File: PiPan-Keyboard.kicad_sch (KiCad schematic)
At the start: 89 parts

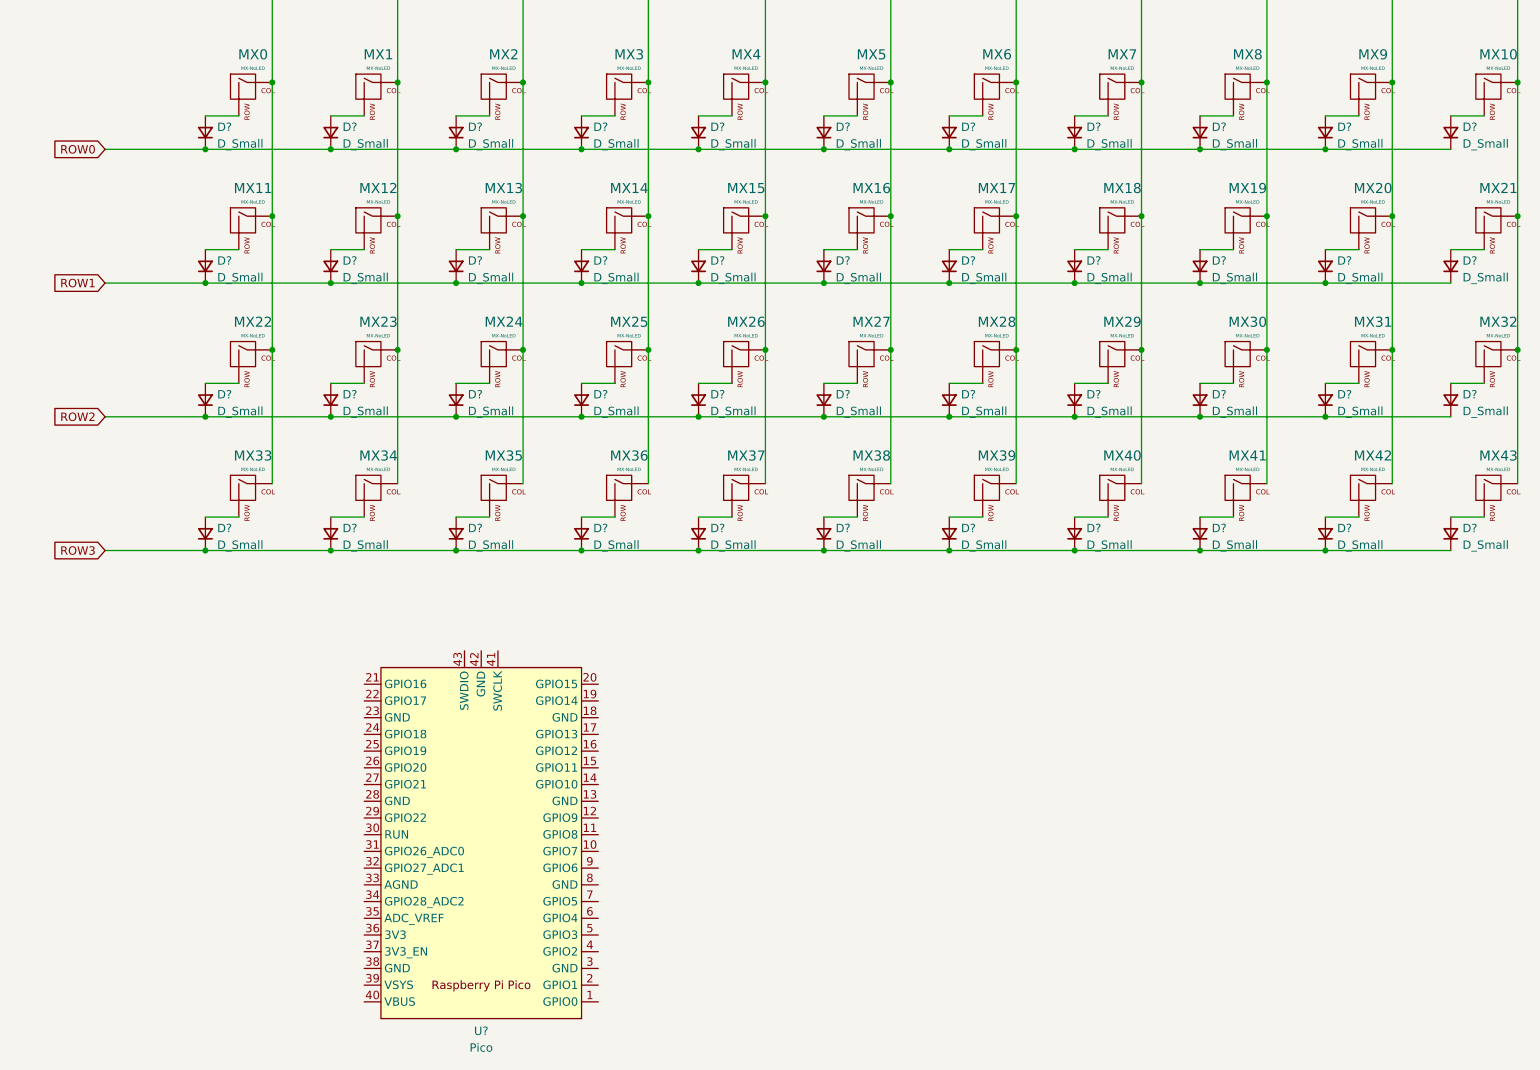
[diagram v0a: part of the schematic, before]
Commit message: added footprints
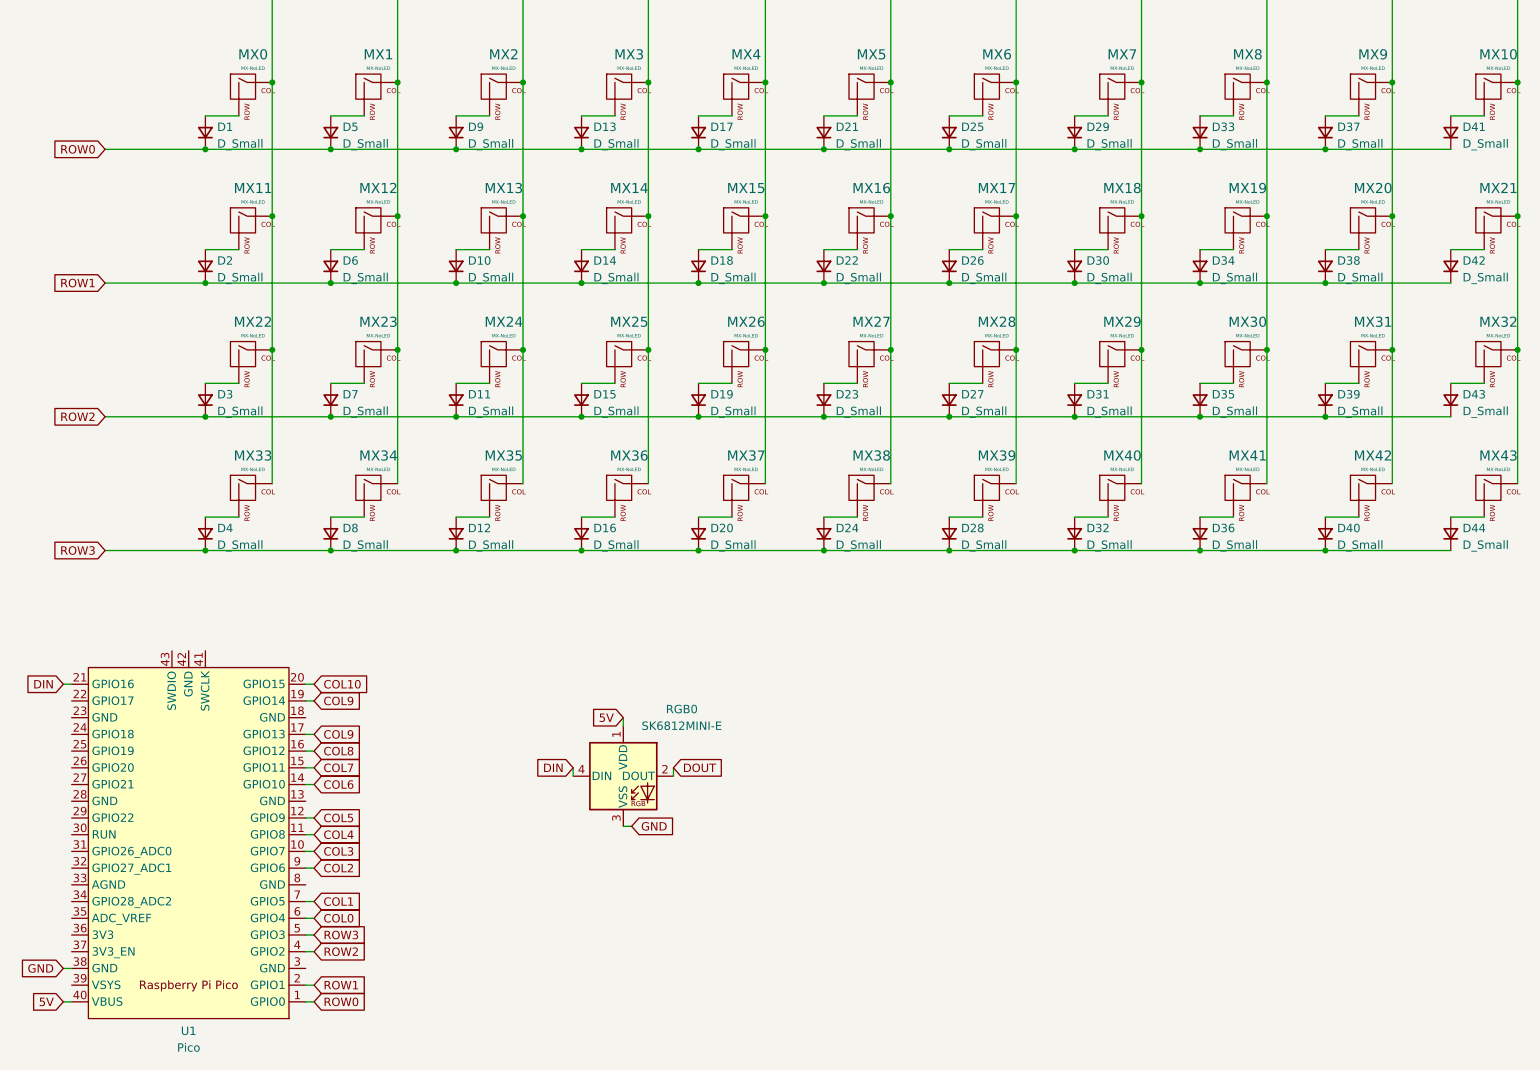
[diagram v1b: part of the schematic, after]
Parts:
- added RGB0: SK6812MINI-E, kicad-keyboard-parts:MX_SK6812MINI-E, symbol kicad-keyboard-parts:SK6812MINI-E
- D1, D10, D11, D12, D13, D14, D15, D16, D17, D18, D19, D2, D20, D21, D22, D23, D24, D25, D26, D27, D28, D29, D3, D30, D31, D32, D33, D34, D35, D36, D37, D38, D39, D4, D40, D41, D42, D43, D44, D5, D6, D7, D8, D9: renamed from D?; footprint (none) -> Diode_THT:D_DO-35_SOD27_P10.16mm_Horizontal
- MX0, MX1, MX10, MX11, MX12, MX13, MX14, MX15, MX16, MX17, MX18, MX19, MX2, MX20, MX21, MX22, MX23, MX24, MX25, MX26, MX27, MX28, MX29, MX3, MX30, MX31, MX32, MX33, MX34, MX35, MX36, MX37, MX38, MX39, MX4, MX40, MX41, MX42, MX43, MX5, MX6, MX7, MX8, MX9: footprint (none) -> keyswitches:Kailh_socket_MX
- U1: renamed from U?; footprint RPi_Pico:RPi_Pico_SMD_TH -> MCU_RaspberryPi_and_Boards:RPi_Pico_SMD_TH
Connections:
- net COL0: now also U1.6 (GPIO4)
- net COL1: now also U1.7 (GPIO5)
- net COL10: now also U1.20 (GPIO15)
- net COL2: now also U1.9 (GPIO6)
- net COL3: now also U1.10 (GPIO7)
- net COL4: now also U1.11 (GPIO8)
- net COL5: now also U1.12 (GPIO9)
- net COL6: now also U1.14 (GPIO10)
- net COL7: now also U1.15 (GPIO11)
- net COL8: now also U1.16 (GPIO12)
- net COL9: now also U1.17 (GPIO13), U1.19 (GPIO14)
- net ROW0: now also U1.1 (GPIO0)
- net ROW1: now also U1.2 (GPIO1)
- net ROW2: now also U1.4 (GPIO2)
- net ROW3: now also U1.5 (GPIO3)
- net DIN: now reaches U1.21 (GPIO16)
- net DIN: now also RGB0.4 (DIN)
- net GND: now reaches U1.38 (GND)
- net GND: now also RGB0.3 (VSS)
- net 5V: now reaches U1.40 (VBUS)
- net 5V: now also RGB0.1 (VDD)
- new net DOUT: RGB0.2 (DOUT)
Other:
- moved on the sheet: U1

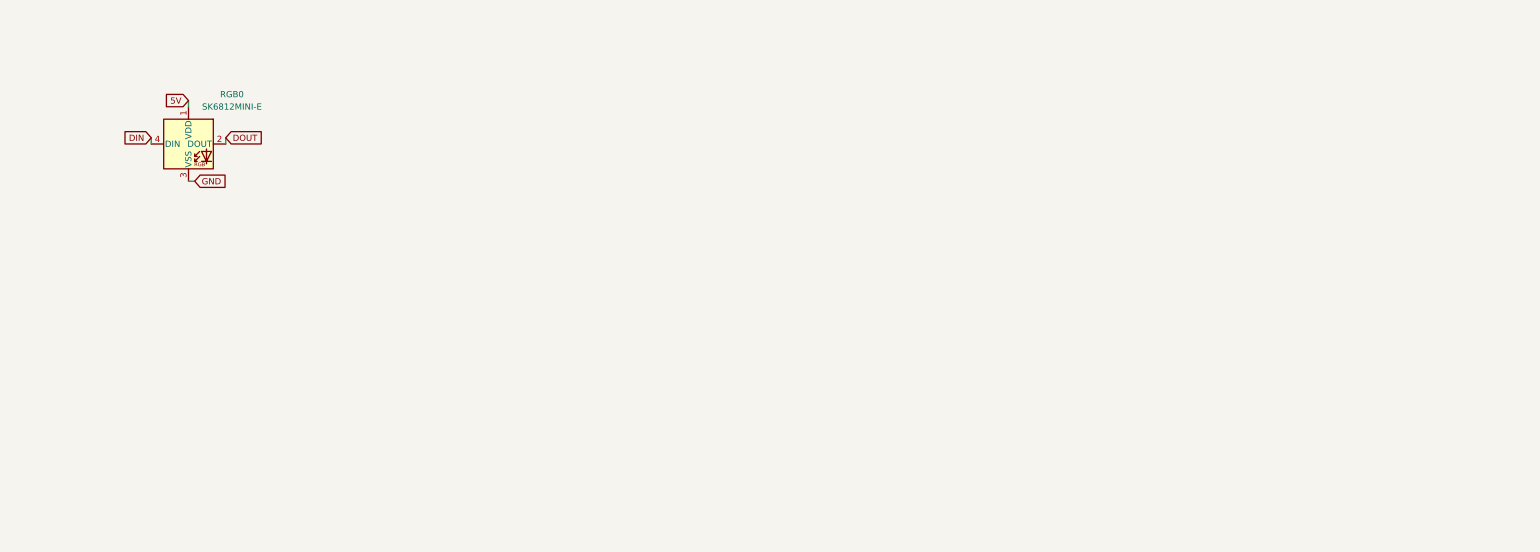
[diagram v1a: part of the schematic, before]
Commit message: added RGB LEDs to schematic
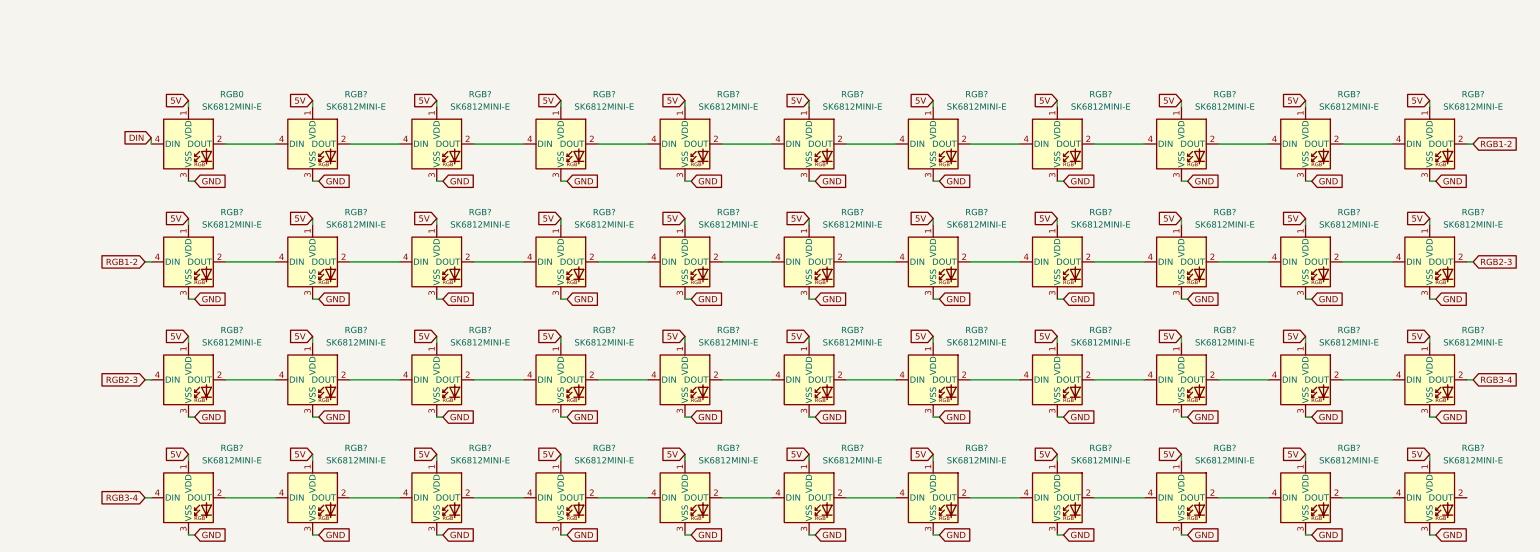
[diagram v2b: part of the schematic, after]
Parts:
- added RGB? (x43): SK6812MINI-E, kicad-keyboard-parts:MX_SK6812MINI-E, symbol kicad-keyboard-parts:SK6812MINI-E
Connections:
- net 5V: now also RGB?.1 (VDD), RGB?.1 (VDD), RGB?.1 (VDD), RGB?.1 (VDD), RGB?.1 (VDD), RGB?.1 (VDD), RGB?.1 (VDD), RGB?.1 (VDD), RGB?.1 (VDD), RGB?.1 (VDD), RGB?.1 (VDD), RGB?.1 (VDD), RGB?.1 (VDD), RGB?.1 (VDD), RGB?.1 (VDD), RGB?.1 (VDD), RGB?.1 (VDD), RGB?.1 (VDD), RGB?.1 (VDD), RGB?.1 (VDD), RGB?.1 (VDD), RGB?.1 (VDD), RGB?.1 (VDD), RGB?.1 (VDD), RGB?.1 (VDD), RGB?.1 (VDD), RGB?.1 (VDD), RGB?.1 (VDD), RGB?.1 (VDD), RGB?.1 (VDD), RGB?.1 (VDD), RGB?.1 (VDD), RGB?.1 (VDD), RGB?.1 (VDD), RGB?.1 (VDD), RGB?.1 (VDD), RGB?.1 (VDD), RGB?.1 (VDD), RGB?.1 (VDD), RGB?.1 (VDD), RGB?.1 (VDD), RGB?.1 (VDD), RGB?.1 (VDD)
- net GND: now also RGB?.3 (VSS), RGB?.3 (VSS), RGB?.3 (VSS), RGB?.3 (VSS), RGB?.3 (VSS), RGB?.3 (VSS), RGB?.3 (VSS), RGB?.3 (VSS), RGB?.3 (VSS), RGB?.3 (VSS), RGB?.3 (VSS), RGB?.3 (VSS), RGB?.3 (VSS), RGB?.3 (VSS), RGB?.3 (VSS), RGB?.3 (VSS), RGB?.3 (VSS), RGB?.3 (VSS), RGB?.3 (VSS), RGB?.3 (VSS), RGB?.3 (VSS), RGB?.3 (VSS), RGB?.3 (VSS), RGB?.3 (VSS), RGB?.3 (VSS), RGB?.3 (VSS), RGB?.3 (VSS), RGB?.3 (VSS), RGB?.3 (VSS), RGB?.3 (VSS), RGB?.3 (VSS), RGB?.3 (VSS), RGB?.3 (VSS), RGB?.3 (VSS), RGB?.3 (VSS), RGB?.3 (VSS), RGB?.3 (VSS), RGB?.3 (VSS), RGB?.3 (VSS), RGB?.3 (VSS), RGB?.3 (VSS), RGB?.3 (VSS), RGB?.3 (VSS)
- net DOUT: no longer names the net of RGB0.2 (DOUT)
- net DOUT: now also RGB?.4 (DIN)
- new net: RGB?.2 (DOUT), RGB?.4 (DIN) (x39)
- new net RGB1-2: RGB?.2 (DOUT), RGB?.4 (DIN)
- new net RGB2-3: RGB?.2 (DOUT), RGB?.4 (DIN)
- new net RGB3-4: RGB?.2 (DOUT), RGB?.4 (DIN)

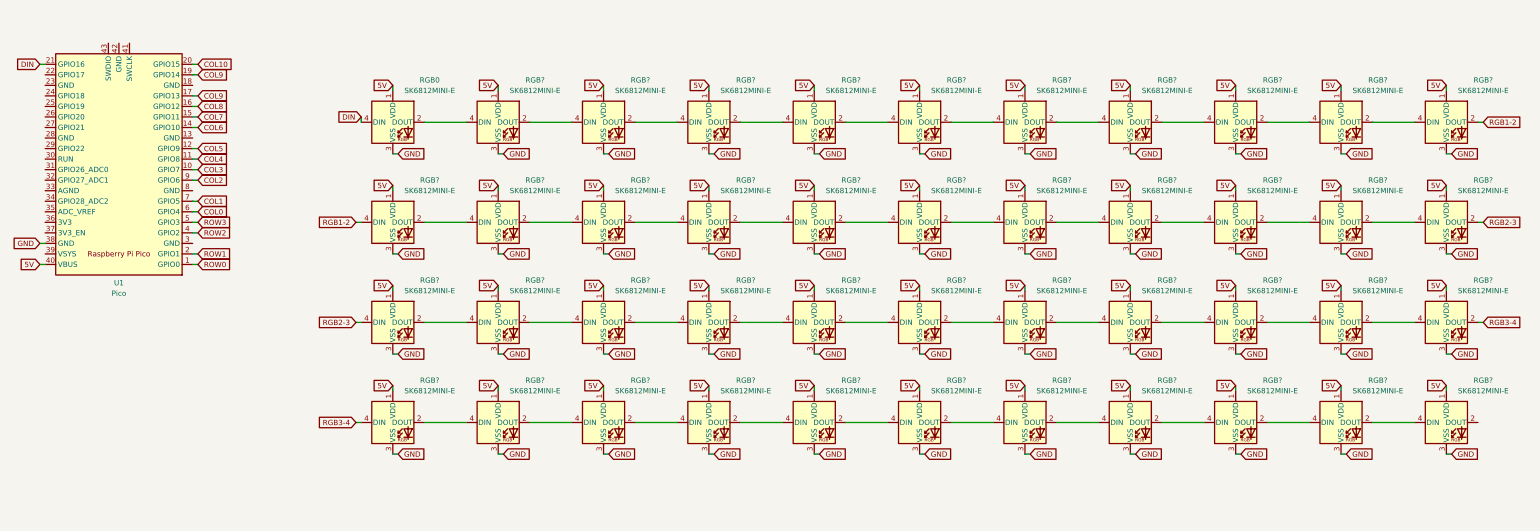
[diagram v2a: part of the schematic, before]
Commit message: added libs and encoder and oled
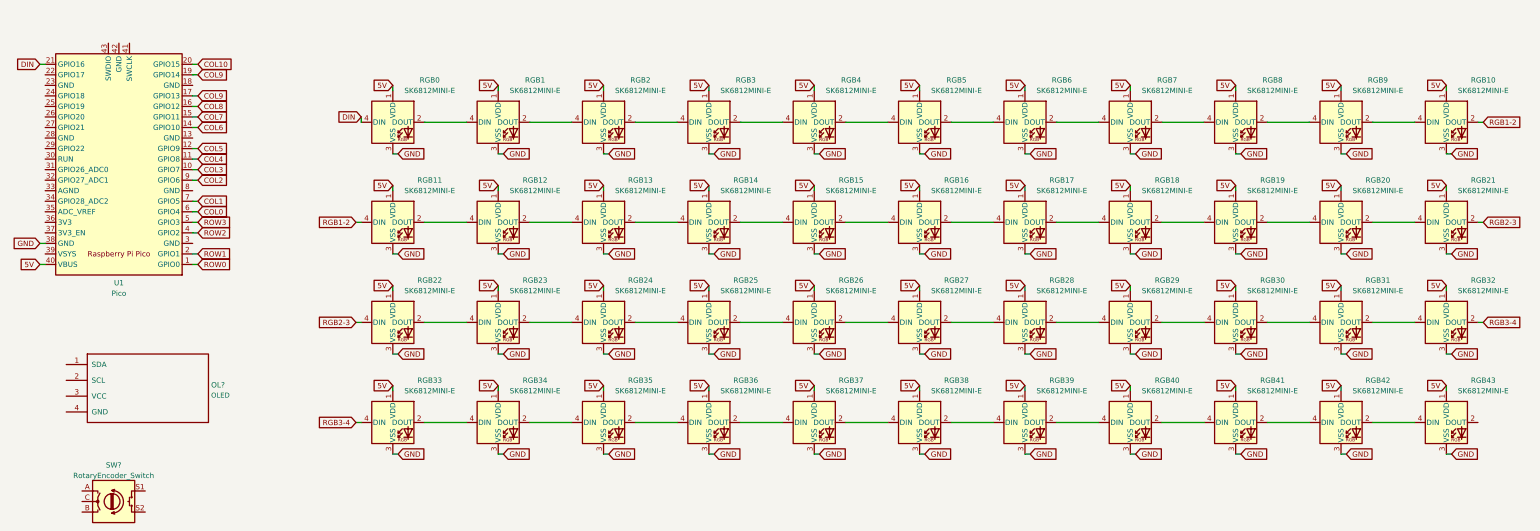
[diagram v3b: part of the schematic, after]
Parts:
- added OL?: OLED, symbol kbd:OLED
- added SW?: RotaryEncoder_Switch, symbol Device:RotaryEncoder_Switch
- gave numbers to parts that had none: 43

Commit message: updated definitions
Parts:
- added D45: D_Small, Diode_THT:D_DO-35_SOD27_P10.16mm_Horizontal, symbol Device:D_Small
- added J0: Conn_01x18_MountingPin, Connector_PinSocket_2.54mm:PinSocket_1x14_P2.54mm_Vertical, symbol Connector_Generic_MountingPin:Conn_01x14_MountingPin
- OL1: renamed from OL?; footprint (none) -> Connector_PinSocket_2.54mm:PinSocket_1x04_P2.54mm_Horizontal
- SW0: renamed from SW?; footprint (none) -> Rotary_Encoder:RotaryEncoder_Alps_EC11E-Switch_Vertical_H20mm
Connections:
- net 5V: now also OL1.3 (VCC), J0.2 (Pin_2)
- net DIN: now also U1.29 (GPIO22); no longer U1.21 (GPIO16)
- net GND: now also OL1.4 (GND), SW0.C, J0.1 (Pin_1)
- net ROW0: now also D45.1 (K)
- net I2C1-SDA: now reaches OL1.1 (SDA)
- net I2C1-SDA: now also OL1.2 (SCL), U1.31 (GPIO26_ADC0), U1.32 (GPIO27_ADC1)
- net PIN_22: now reaches U1.22 (GPIO17)
- net PIN_22: now also J0.11 (Pin_11)
- net PIN_24: now reaches U1.24 (GPIO18)
- net PIN_24: now also J0.10 (Pin_10)
- net PIN_25: now reaches U1.25 (GPIO19)
- net PIN_25: now also J0.9 (Pin_9)
- net Encoder_B: now reaches U1.26 (GPIO20)
- net Encoder_B: now also SW0.B
- net Encoder_A: now reaches U1.27 (GPIO21)
- net Encoder_A: now also SW0.A
- net PIN_30: now reaches U1.30 (RUN)
- net PIN_30: now also J0.8 (Pin_8)
- net PIN_33: now reaches U1.33 (AGND)
- net PIN_33: now also J0.7 (Pin_7)
- net PIN_34: now reaches U1.34 (GPIO28_ADC2)
- net PIN_34: now also J0.6 (Pin_6)
- net PIN_35: now reaches U1.35 (ADC_VREF)
- net PIN_35: now also J0.5 (Pin_5)
- net PIN_36: now reaches U1.36 (3V3)
- net PIN_36: now also J0.4 (Pin_4)
- net PIN_37: now reaches U1.37 (3V3_EN)
- net PIN_37: now also J0.3 (Pin_3)
- net PIN_41: now reaches U1.41 (SWCLK)
- net PIN_41: now also J0.13 (Pin_13)
- net PIN_43: now reaches U1.43 (SWDIO)
- net PIN_43: now also J0.14 (Pin_14)
- net at SW0.S1: now also D45.2 (A)
- net COL11: now reaches SW0.S2
- net RGB1-2: no longer names the net of RGB10.2 (DOUT)
- net RGB1-2: no longer RGB11.4 (DIN)
- net RGB2-3 renamed RGB2>3
- net RGB3-4 renamed RGB3>4
- new net PIN_21: J0.12 (Pin_12), U1.21 (GPIO16)
- new net RGB1>2: RGB11.4 (DIN)
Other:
- moved on the sheet: D1, D10, D11, D12, D13, D14, D15, D16, D17, D18, D19, D2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
